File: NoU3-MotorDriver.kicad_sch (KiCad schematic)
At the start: 9 parts, among them J7 Screw_Terminal_01x02, J8 Screw_Terminal_01x02

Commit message: finished main changes, just need to route now
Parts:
- removed J7: Screw_Terminal_01x02, AlfredoFootprints:TerminalBlock_Ningbo_2P_5mm, symbol Connector:Screw_Terminal_01x02
- removed J?: JST SR/SZ, Connector_JST:JST_SH_BM06B-SRSS-TB_1x06-1MP_P1.00mm_Vertical, symbol Connector_Generic:Conn_01x06
- removed R?: 22K, Resistor_SMD:R_0402_1005Metric, symbol Device:R
- added J9: Screw_Terminal_01x02, AlfredoFootprints:TerminalBlock_Ningbo_2P_5mm, symbol Connector:Screw_Terminal_01x02
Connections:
- net nSleep: now reaches U?.1 (nSLEEP)
- net Aout1: now reaches U?.2 (AOUT1)
- net Aout1: now also J8.2 (Pin_2)
- net Aout2: now reaches U?.4 (AOUT2)
- net Aout2: now also J8.1 (Pin_1)
- net Bout2: now reaches U?.5 (BOUT2)
- net Bout2: now also J9.2 (Pin_2); no longer J8.2 (Pin_2)
- net Bout1: now reaches U?.7 (BOUT1)
- net Bout1: now also J9.1 (Pin_1); no longer J8.1 (Pin_1)

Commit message: NoU3 as ordered 8/7/23
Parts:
- R?: LCSC C270655 -> C346796
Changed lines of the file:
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@@
       (effects (font (size 1.27 1.27)) hide)
     )
-    (property "Datasheet" "https://jlcpcb.com/partdetail/260035-0402WGF100LTCE/C270655" (at 137.16 91.44 0)
+    (property "Datasheet" "https://www.lcsc.com/product-detail/Current-Sense-Resistors-Shunt-Resistors_SEIStackpole-Elec-SEIStackpole-Elec-CSR0402FKR100_C346796.html" (at 137.16 91.44 0)
       (effects (font (size 1.27 1.27)) hide)
     )
-    (property "LCSC" "C270655" (at 137.16 91.44 0)
+    (property "LCSC" "C346796" (at 137.16 91.44 0)
       (effects (font (size 1.27 1.27)) hide)
     )

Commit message: initial V3.2 changes
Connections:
- net nSleep: no longer names the net of U?.1 (nSLEEP)
- no-connect marks 0 -> 1
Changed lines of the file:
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@@
   (junction (at 187.96 104.14) (diameter 0) (color 0 0 0 0)
   )
+  (no_connect (at 171.45 91.44))
   (wire (pts (xy 158.75 111.76) (xy 156.21 111.76))
     (stroke (width 0) (type default))
@@
     (effects (font (size 1.27 1.27)) (justify left))
   )
-  (hierarchical_label "nSleep" (shape input) (at 140.97 73.66 180) (fields_autoplaced)
-    (effects (font (size 1.27 1.27)) (justify right))
-  )
   (hierarchical_label "AIN2" (shape input) (at 138.43 99.06 180) (fields_autoplaced)

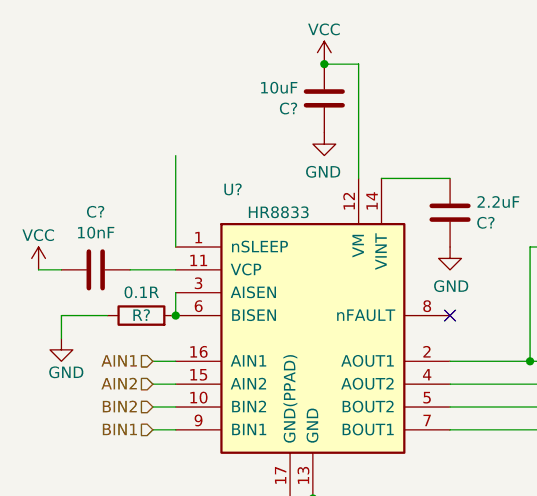
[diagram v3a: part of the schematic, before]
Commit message: order candidate, layout complete
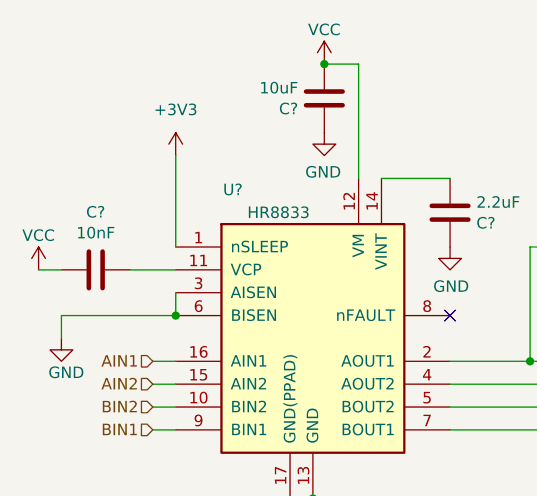
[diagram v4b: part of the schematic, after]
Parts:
- removed R?: 0.1R, Resistor_SMD:R_0402_1005Metric, symbol Device:R
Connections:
- net GND: now also U?.3 (AISEN), U?.6 (BISEN)
- net +3V3: now reaches U?.1 (nSLEEP)
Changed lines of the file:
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@@
   (junction (at 157.48 63.5) (diameter 0) (color 0 0 0 0)
   )
+  (junction (at 156.21 111.76) (diameter 0) (color 0 0 0 0)
+  )
+  (junction (at 180.34 96.52) (diameter 0) (color 0 0 0 0)
+  )
   (junction (at 140.97 91.44) (diameter 0) (color 0 0 0 0)
   )
-  (junction (at 156.21 111.76) (diameter 0) (color 0 0 0 0)
-  )
-  (junction (at 180.34 96.52) (diameter 0) (color 0 0 0 0)
-  )
   (junction (at 185.42 101.6) (diameter 0) (color 0 0 0 0)
   )
@@
   )
   (no_connect (at 171.45 91.44))
+  (wire (pts (xy 128.27 91.44) (xy 140.97 91.44))
+    (stroke (width 0) (type default))
+  )
   (wire (pts (xy 158.75 111.76) (xy 156.21 111.76))
     (stroke (width 0) (type default))
@@
   )
   (wire (pts (xy 138.43 99.06) (xy 140.97 99.06))
-    (stroke (width 0) (type default))
-  )
-  (wire (pts (xy 128.27 91.44) (xy 133.35 91.44))
     (stroke (width 0) (type default))
   )
@@
         (path "/e83aa78a-7ee8-4825-a22a-a2646798082a/1f426c13-9812-4a54-acf9-8bfc20256e33"
           (reference "#PWR016") (unit 1)
+        )
+      )
+    )
+  )
+  (symbol (lib_id "power:+3V3") (at 140.97 73.66 0) (unit 1)
+    (in_bom yes) (on_board yes) (dnp no) (fields_autoplaced)
+    (property "Reference" "#PWR053" (at 140.97 77.47 0)
+      (effects (font (size 1.27 1.27)) hide)
+    )
+    (property "Value" "+3V3" (at 140.97 68.58 0)
+      (effects (font (size 1.27 1.27)))
+    )
+    (property "Footprint" "" (at 140.97 73.66 0)
+      (effects (font (size 1.27 1.27)) hide)
+    )
+    (property "Datasheet" "" (at 140.97 73.66 0)
+      (effects (font (size 1.27 1.27)) hide)
+    )
+    (pin "1")
+    (instances
+      (project "NoU3"
+        (path "/e83aa78a-7ee8-4825-a22a-a2646798082a/96418c08-a60c-47ec-aa14-bc1c55e3c924"
+          (reference "#PWR053") (unit 1)
+        )
+        (path "/e83aa78a-7ee8-4825-a22a-a2646798082a/9d00c82b-a63d-48c8-a087-ca03e0f7b83a"
+          (reference "#PWR013") (unit 1)
+        )
+        (path "/e83aa78a-7ee8-4825-a22a-a2646798082a/1f426c13-9812-4a54-acf9-8bfc20256e33"
+          (reference "#PWR052") (unit 1)
+        )
+        (path "/e83aa78a-7ee8-4825-a22a-a2646798082a/3894b403-fba6-471e-ab0a-253efe7a8dae"
+          (reference "#PWR054") (unit 1)
         )
       )
@@
         )
       )
-    )
-  )
-  (symbol (lib_id "Device:R") (at 137.16 91.44 90) (unit 1)
-    (in_bom yes) (on_board yes) (dnp no)
-    (property "Reference" "R?" (at 137.16 91.44 90)
-      (effects (font (size 1.27 1.27)))
-    )
-    (property "Value" "0.1R" (at 137.16 88.9 90)
-      (effects (font (size 1.27 1.27)))
-    )
-    (property "Footprint" "Resistor_SMD:R_0402_1005Metric" (at 137.16 93.218 90)
-      (effects (font (size 1.27 1.27)) hide)
-    )
-    (property "Datasheet" "https://www.lcsc.com/product-detail/Current-Sense-Resistors-Shunt-Resistors_SEIStackpole-Elec-SEIStackpole-Elec-CSR0402FKR100_C346796.html" (at 137.16 91.44 0)
-      (effects (font (size 1.27 1.27)) hide)
-    )
-    (property "LCSC" "C346796" (at 137.16 91.44 0)
-      (effects (font (size 1.27 1.27)) hide)
-    )
-    (pin "1")
-    (pin "2")
-    (instances
-      (project "NoU3"
-        (path "/e83aa78a-7ee8-4825-a22a-a2646798082a"
-          (reference "R?") (unit 1)
-        )
-        (path "/e83aa78a-7ee8-4825-a22a-a2646798082a/96418c08-a60c-47ec-aa14-bc1c55e3c924"
-          (reference "R6") (unit 1)
-        )
-        (path "/e83aa78a-7ee8-4825-a22a-a2646798082a/3894b403-fba6-471e-ab0a-253efe7a8dae"
-          (reference "R8") (unit 1)
-        )
-        (path "/e83aa78a-7ee8-4825-a22a-a2646798082a/9d00c82b-a63d-48c8-a087-ca03e0f7b83a"
-          (reference "R1") (unit 1)
-        )
-        (path "/e83aa78a-7ee8-4825-a22a-a2646798082a/1f426c13-9812-4a54-acf9-8bfc20256e33"
-          (reference "R3") (unit 1)
-        )
-      )

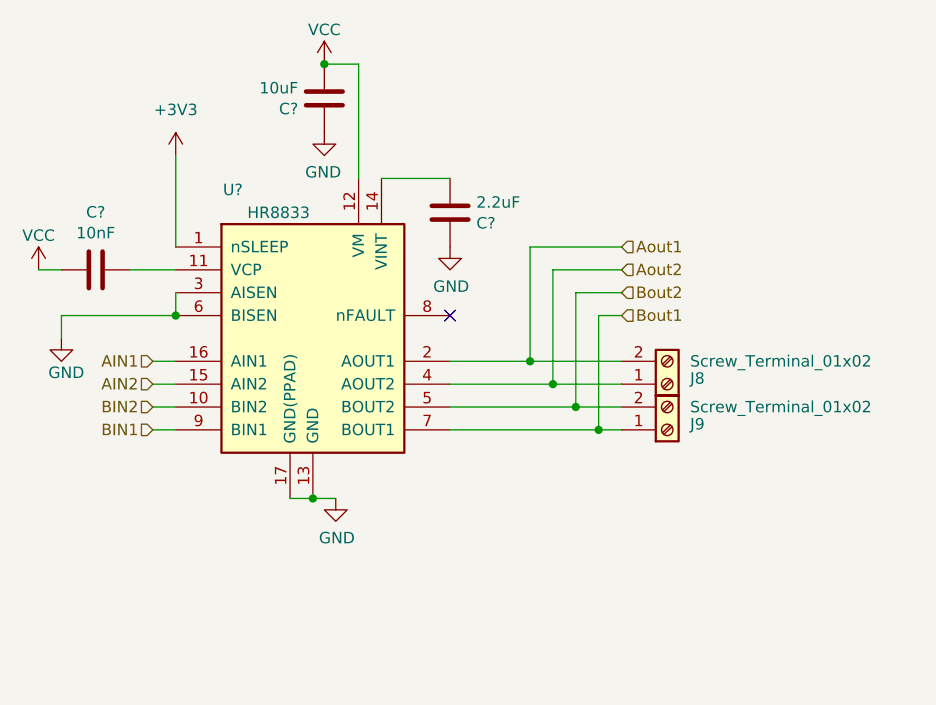
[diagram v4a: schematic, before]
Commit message: used a different fabrication tool
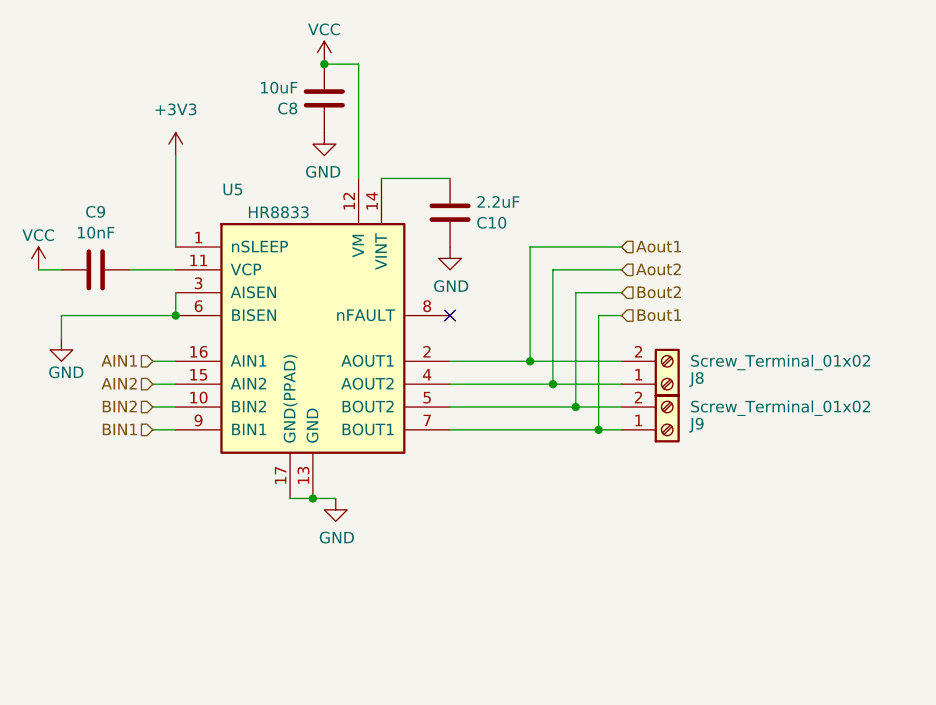
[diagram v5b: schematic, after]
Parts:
- gave numbers to parts that had none: 4

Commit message: Schematic cleanup and plotted PDF
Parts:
- renumbered C8 to C2, C9 to C3, C10 to C4, J8 to J2, J9 to J3, U5 to U1

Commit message: updated labels
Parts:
- J2, J3: LCSC C557646 -> C8404
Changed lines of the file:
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@@
 			)
 		)
-		(property "Datasheet" "https://www.lcsc.com/product-detail/Screw-terminal_Ningbo-Xinlaiya-Elec.-Ningbo-Xinlaiya-Elec.-XY126V-5.0-2P_C557646.html"
+		(property "Datasheet" ""
 			(at 195.58 104.14 0)
 			(effects
@@
 			)
 		)
-		(property "LCSC" "C557646"
+		(property "LCSC" "C8404 "
 			(at 195.58 104.14 0)
 			(effects
@@
 			)
 		)
-		(property "Datasheet" "https://www.lcsc.com/product-detail/Screw-terminal_Ningbo-Xinlaiya-Elec.-Ningbo-Xinlaiya-Elec.-XY126V-5.0-2P_C557646.html"
+		(property "Datasheet" ""
 			(at 195.58 99.06 0)
 			(effects
@@
 			)
 		)
-		(property "LCSC" "C557646"
+		(property "LCSC" "C8404 "
 			(at 195.58 99.06 0)
 			(effects
